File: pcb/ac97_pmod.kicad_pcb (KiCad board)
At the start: 2 copper layers, 34 x 48 mm, 48 parts, among them J301 JACK_TRRS_6PINS, P301 RCA_2, P302 RCA_2, P401 CONN_02X06, U201 MCP1640-*/CHY, U301 LM4550, X301 24MHz

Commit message: added schematic
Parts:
- added C318: 2.2u, Capacitors_SMD:C_0805, F.Cu at (170.0, 117.5)
- added C319: 2.2u, Capacitors_SMD:C_0805, F.Cu at (152.0, 118.5)
- added C320: 2.2u, Capacitors_SMD:C_0805, F.Cu at (170.0, 120.0)
- added R316: 10k, Resistors_SMD:R_0805, F.Cu at (174.0, 120.0)
- P401: footprint Pin_Headers:Pin_Header_Angled_2x06 -> Pin_Headers:Pin_Header_Straight_2x06
- moved L201 115.2 mm to (147.5, 130.5), turned to 180 degrees
- moved C201 114.1 mm to (144.0, 135.0), turned to 90 degrees
- moved R201 109.6 mm to (151.5, 138.5), turned to 90 degrees
- moved FB201 109.1 mm to (153.5, 133.5), turned to 90 degrees
- moved U201 103.4 mm to (147.5, 134.5)
- moved C202 102.1 mm to (151.0, 133.5), turned to 90 degrees
- moved R202 96.8 mm to (149.0, 138.5), turned to 270 degrees
- moved C203 92.9 mm to (156.0, 133.5), turned to 270 degrees
- moved C305 82.6 mm to (152.0, 106.0), turned to 180 degrees
- moved C302 80.1 mm to (152.0, 116.0)
- moved C311 75.6 mm to (159.5, 146.5), turned to 180 degrees
- moved R305 74.4 mm to (156.0, 102.5), turned to 180 degrees
- moved C308 70.5 mm to (158.5, 122.0), turned to 180 degrees
- moved C303 69.6 mm to (164.0, 105.0), turned to 180 degrees
- moved R306 67.4 mm to (156.0, 105.0), turned to 180 degrees
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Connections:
- J301 pad 5: Net-(J301-Pad5) -> (no net)
- J301 pad 6: Net-(J301-Pad6) -> (no net)
- P401 pad 1: Net-(P401-Pad1) -> (no net)
- P401 pad 2: Net-(P401-Pad2) -> (no net)
- P401 pad 4: Net-(P401-Pad4) -> (no net)
- U301 pad 1: (no net) -> +3V3
- U301 pad 25: (no net) -> +5V
- U301 pad 26: (no net) -> GND
- U301 pad 27: (no net) -> Net-(C318-Pad1)
- U301 pad 4: (no net) -> GND
- U301 pad 7: (no net) -> GND
- U301 pad 9: (no net) -> +3V3
- X301 pad 1: Net-(C302-Pad2) -> Net-(C305-Pad2)
- X301 pad 3: Net-(C305-Pad2) -> Net-(C302-Pad2)
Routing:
- net /AC97/phone_r_out: track 0.00 -> 47.3 mm, vias 0 -> 2
- net GND: track 0.00 -> 39.2 mm, vias 0 -> 28
- net /AC97/phone_l_out: track 0.00 -> 38.3 mm, vias 0 -> 2
- net /AC97/phone_right: track 0.00 -> 29.7 mm
- net /AC97/LINE_OUT_R: track 0.00 -> 28.2 mm, vias 0 -> 2
- net /PMOD Connector/RESET: track 0.00 -> 28.0 mm
- net +3V3: track 0.00 -> 27.9 mm, vias 0 -> 9
- net /AC97/mic: track 0.00 -> 27.8 mm
- net /AC97/LINE_OUT_L: track 0.00 -> 22.7 mm, vias 0 -> 2
- net /AC97/DIN: track 0.00 -> 21.3 mm, vias 0 -> 1
- net /AC97/DOUT: track 0.00 -> 20.0 mm, vias 0 -> 1
- net +5V: track 0.00 -> 19.2 mm, vias 0 -> 3
- net /AC97/SYNC: track 0.00 -> 18.2 mm, vias 0 -> 2
- net /AC97/LINE_IN_L: track 0.00 -> 18.1 mm, vias 0 -> 2
- net /AC97/CLK: track 0.00 -> 17.5 mm, vias 0 -> 1
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- added copper zone on In2.Cu, net +3V3
- added copper zone on In2.Cu, net +5V
- added copper zone on In1.Cu, net GND
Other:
- board size 34 x 48 mm -> 50 x 50 mm
- copper layers 2 -> 4
- net class Default: clearance 0.2 -> 0.16; trace_width 0.25 -> 0.16; via_dia 0.6 -> 0.72; via_drill 0.4 -> 0.31
- rule pad_to_mask_clearance: 0.2 -> 0.05
- rule trace_clearance: 0.2 -> 0.16
- rule trace_min: 0.2 -> 0.16
- rule via_min_drill: 0.3 -> 0.31
- rule via_min_size: 0.4 -> 0.72
- board text added: "AC97 Breakout Board wbraun@mit.edu"
- board text added: "IN"
- board text added: "OUT"

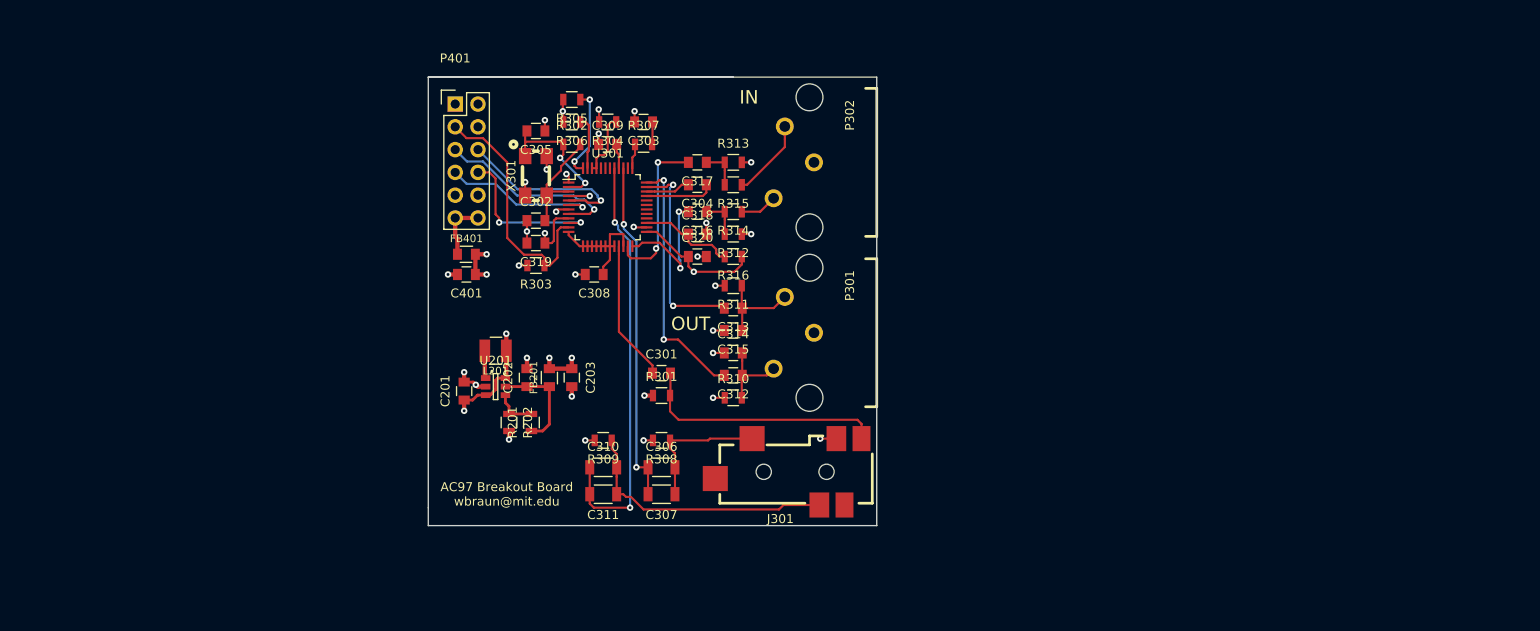
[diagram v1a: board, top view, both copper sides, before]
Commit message: replaced ceramic DC blocking caps with electrolytics
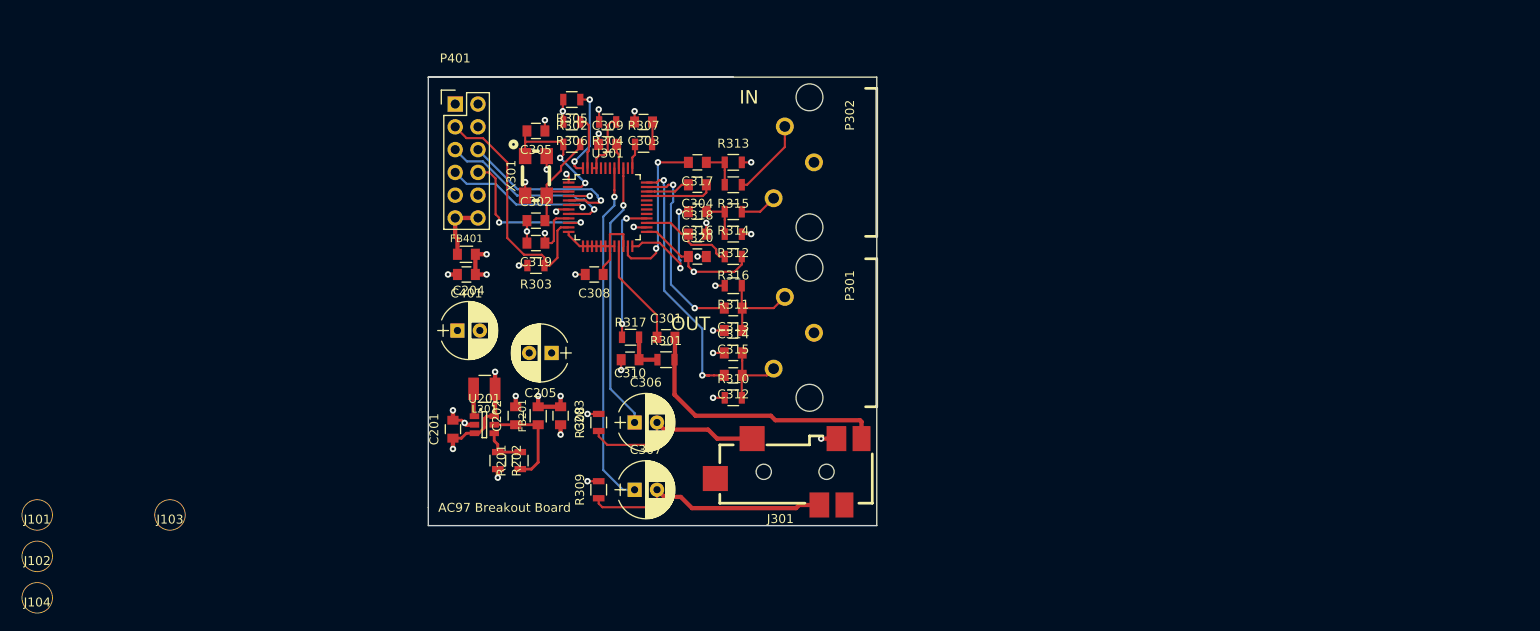
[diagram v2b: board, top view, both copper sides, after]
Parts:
- removed C311: 47u, Capacitors_SMD:C_1206
- added C204: CP, Capacitors_ThroughHole:CP_Radial_D6.3mm_P2.50mm, F.Cu at (143.2, 128.2)
- added C205: CP, Capacitors_ThroughHole:CP_Radial_D6.3mm_P2.50mm, F.Cu at (153.8, 130.8)
- added J101: mounting-hole-nc, wbraun_smd:M3-small-mounting-hole, F.Cu at (96.4, 148.8)
- added J102: mounting-hole-nc, wbraun_smd:M3-small-mounting-hole, F.Cu at (96.4, 153.4)
- added J103: mounting-hole-nc, wbraun_smd:M3-small-mounting-hole, F.Cu at (111.2, 148.8)
- added J104: mounting-hole-nc, wbraun_smd:M3-small-mounting-hole, F.Cu at (96.4, 158.1)
- added R317: R, Resistors_SMD:R_0805, F.Cu at (162.6, 129.0)
- C306, C307: value 47u -> CP; footprint Capacitors_SMD:C_1206 -> Capacitors_ThroughHole:CP_Radial_D6.3mm_P2.50mm
- C310: value 47u -> C; footprint Capacitors_SMD:C_1206 -> Capacitors_SMD:C_0805
- moved C310 12.4 mm to (162.5, 131.5), turned to 180 degrees
- moved R308 7.28 mm to (159.0, 138.5), turned to 90 degrees
- moved C306 5.83 mm to (163.0, 138.5)
- moved R309 5.52 mm to (159.0, 146.0), turned to 90 degrees
- moved C201 4.43 mm to (142.8, 139.2)
- moved C202 4.43 mm to (149.8, 137.8)
- moved C203 4.43 mm to (154.8, 137.8)
- moved FB201 4.43 mm to (152.2, 137.8)
- moved L201 4.43 mm to (146.2, 134.8)
- moved R201 4.43 mm to (150.2, 142.8)
- moved R202 4.43 mm to (147.8, 142.8)
- moved U201 4.43 mm to (146.2, 138.8)
- moved C301 4.03 mm to (166.5, 129.0)
- moved R301 4.03 mm to (166.5, 131.5)
- moved C307 3.04 mm to (163.0, 146.0), turned to 0 degrees
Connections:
- C307 pad 1: /AC97/phone_left -> /AC97/phone_r_out
- C307 pad 2: /AC97/phone_l_out -> /AC97/phone_right
- C310 pad 1: /AC97/phone_r_out -> /AC97/mic_bias
- C310 pad 2: /AC97/phone_right -> GND
- J301 pad 5: (no net) -> Net-(J301-Pad5)
- J301 pad 6: (no net) -> Net-(J301-Pad6)
- P401 pad 1: (no net) -> Net-(P401-Pad1)
- P401 pad 2: (no net) -> Net-(P401-Pad2)
- P401 pad 4: (no net) -> Net-(P401-Pad4)
- R301 pad 1: +3V3 -> /AC97/mic_bias
- U301 pad 28: (no net) -> Net-(R317-Pad1)
- U301 pad 29: (no net) -> Net-(U301-Pad29)
- U301 pad 30: (no net) -> Net-(U301-Pad30)
- U301 pad 31: (no net) -> Net-(U301-Pad31)
- U301 pad 32: (no net) -> Net-(U301-Pad32)
- U301 pad 38: (no net) -> Net-(U301-Pad38)
- U301 pad 42: (no net) -> Net-(U301-Pad42)
- U301 pad 43: (no net) -> Net-(U301-Pad43)
- U301 pad 44: (no net) -> Net-(U301-Pad44)
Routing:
- net Net-(R317-Pad1): track 0.00 -> 15.9 mm, vias 0 -> 2
- net /AC97/phone_r_out: track 47.3 -> 38.6 mm, vias 2 -> 1
- net /AC97/phone_l_out: track 38.3 -> 30.1 mm, vias 2 -> 1
- net /AC97/phone_left: track 15.5 -> 20.7 mm
- net /AC97/mic_bias: track 0.00 -> 4.55 mm
- net /AC97/mic_out: track 15.7 -> 11.9 mm
- net /AC97/mic: track 27.8 -> 30.4 mm
- net /AC97/phone_right: track 29.7 -> 27.9 mm
- net GND: track 39.2 -> 40.6 mm, vias 28 -> 29
- net /AC97/LINE_OUT_L: track 22.7 -> 21.7 mm
- net +3V3: track 27.9 -> 26.9 mm, vias 9 -> 8
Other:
- board text added: "AC97 Breakout Board"
- board text removed: "AC97 Breakout Board wbraun@mit.edu"

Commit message: fixed bad schematic symbols due to new kicad version
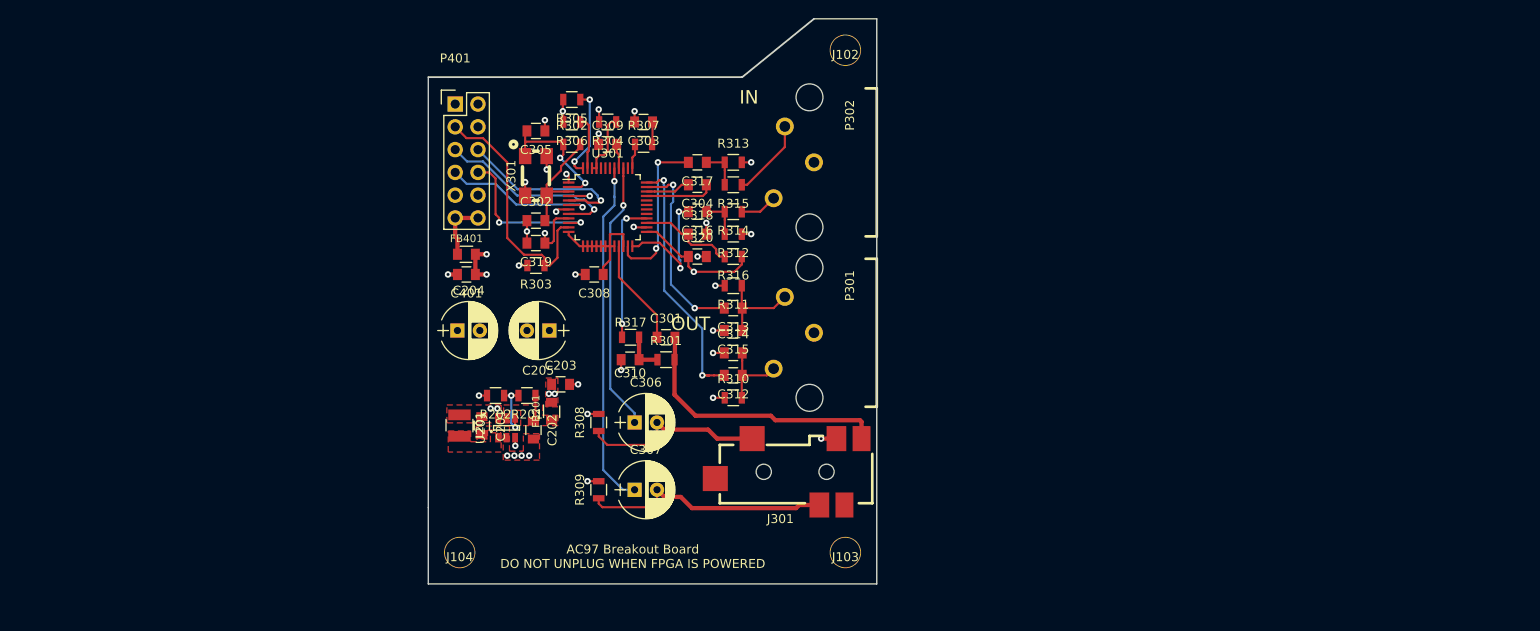
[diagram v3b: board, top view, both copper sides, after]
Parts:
- removed J101: mounting-hole-nc, wbraun_smd:M3-small-mounting-hole
- moved J102 106.3 mm to (186.5, 97.0)
- moved J103 75.4 mm to (186.5, 153.0)
- moved J104 47.4 mm to (143.5, 153.0)
- moved R201 7.29 mm to (151.0, 135.5), turned to 180 degrees
- moved R202 7.25 mm to (147.5, 135.5), turned to 180 degrees
- moved L201 4.95 mm to (143.5, 138.8), turned to 270 degrees
- moved C203 3.50 mm to (154.8, 134.2), turned to 0 degrees
- moved C201 3.25 mm to (146.0, 138.8), turned to 270 degrees
- moved C202 2.54 mm to (151.7, 139.3), turned to 270 degrees
- moved C205 2.51 mm to (153.5, 128.2)
- moved U201 2.50 mm to (148.7, 139.1), turned to 90 degrees
- moved FB201 1.58 mm to (153.8, 137.2)
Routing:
- net +3V3: track 26.9 -> 15.4 mm, vias 8 -> 9
- net Net-(C202-Pad1): track 11.4 -> 2.94 mm
- net GND: track 40.6 -> 35.5 mm, vias 29 -> 30
- net +5V: track 19.2 -> 14.3 mm
- net Net-(L201-Pad2): track 3.09 -> 0.14 mm
- net Net-(R201-Pad2): track 4.77 -> 7.20 mm, vias 0 -> 2
- added copper zone on F.Cu, net +3V3
- added copper zone on F.Cu, net +5V
- added copper zone on F.Cu, net GND
- added copper zone on F.Cu, net Net-(C202-Pad1)
- added copper zone on F.Cu, net Net-(L201-Pad2)
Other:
- board size 50 x 50 mm -> 50 x 63 mm
- rule pad_to_mask_clearance: 0.05 -> 0.06
- board text added: "AC97 Breakout Board DO NOT UNPLUG WHEN FPGA IS POWERED"
- board text removed: "AC97 Breakout Board"
